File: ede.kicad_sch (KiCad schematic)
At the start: 111 parts, among them J1 Conn_01x01, J10 Conn_01x01, J11 Conn_01x01, J12 Conn_01x01, J2 Conn_01x01, J3 Conn_01x01, J4 Conn_01x01, J5 Conn_01x06, J6 Conn_01x01, J7 Conn_01x04, J8 Conn_01x04, J9 Conn_01x01, Q1 MDP10N027, Q2 MDP10N027, Q3 MDP10N027, Q4 MDP10N027, Q5 MDP10N027, Q6 MDP10N027, U1 Blackpill, U2 NCS20034DR2G, U3 STH0548S12, U4 MP1584EN_4pin, U5 U3216, U6 U3216, U7 U3216

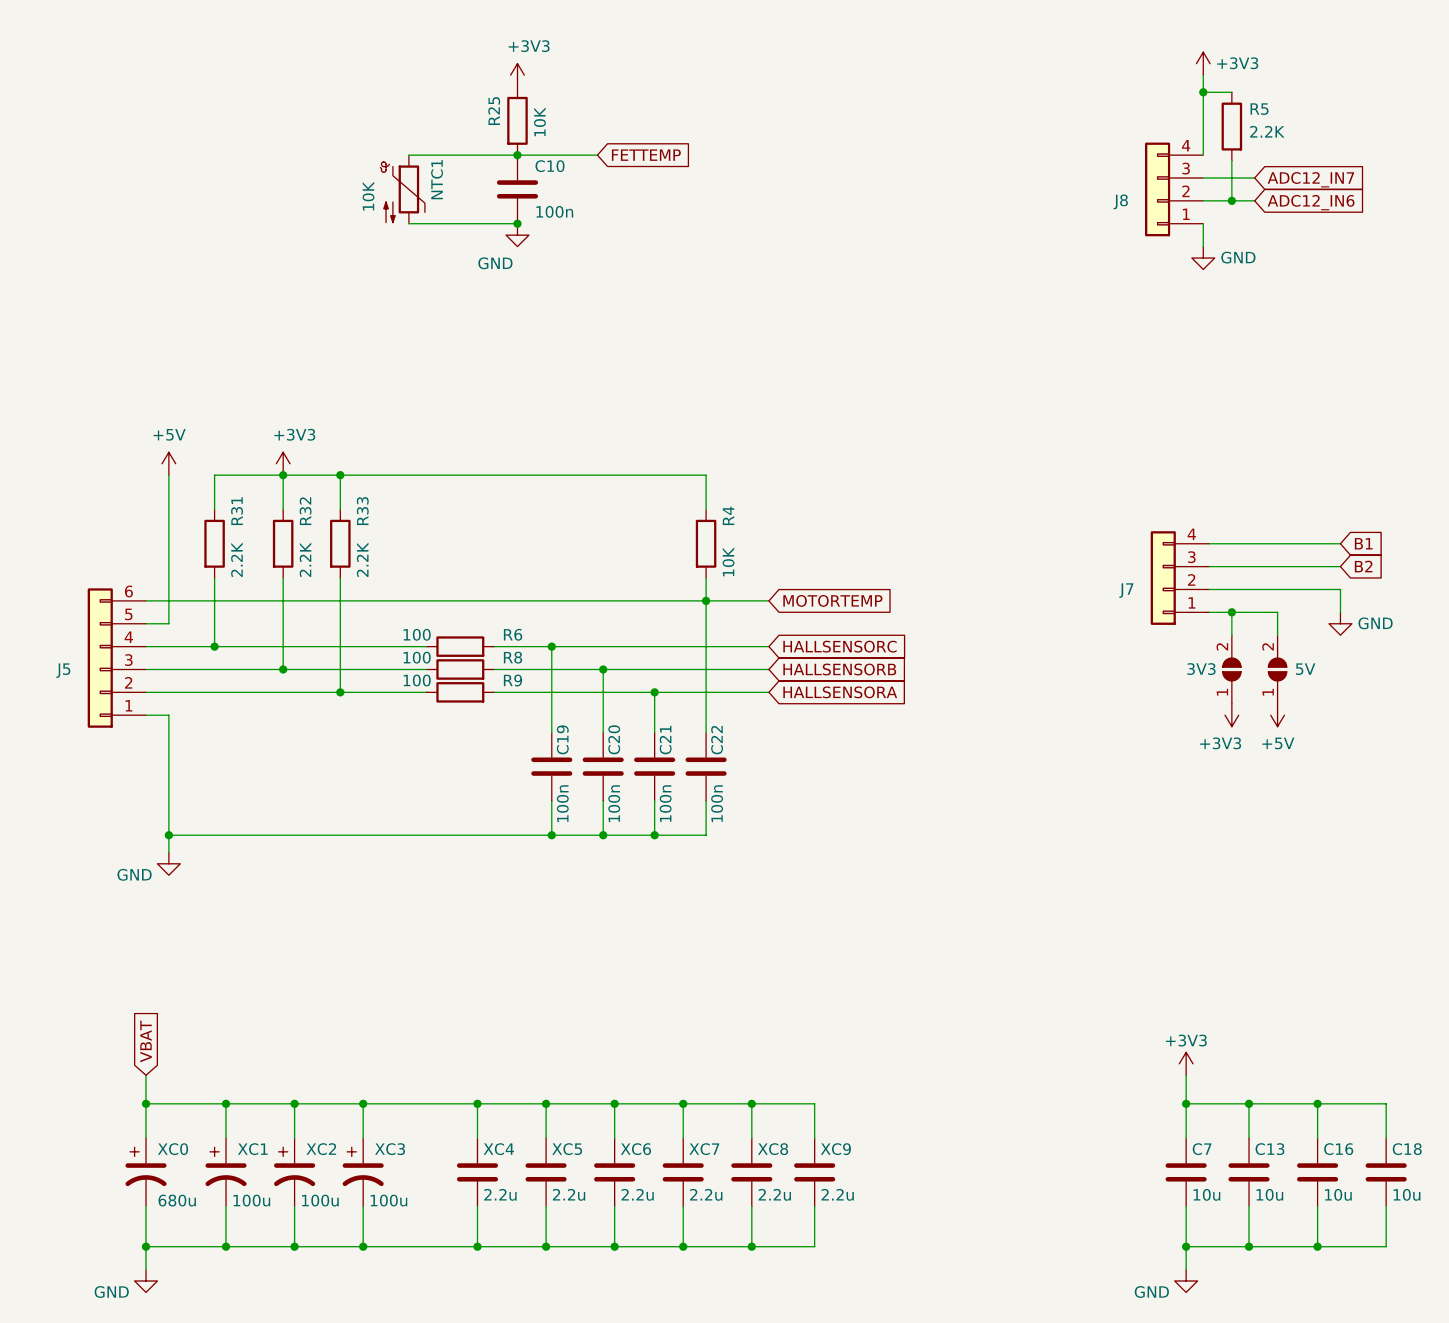
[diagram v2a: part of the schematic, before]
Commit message: KiCad 10 migration
Note: sch & pcb are not in sync, since sch has been changed to represent
blackpill. Though with the existing pcb layout, schematic can be referred,
provided notes mentioned in the schematic are taken into account.

Signed-off-by: Afzal <afzal@intible.in>
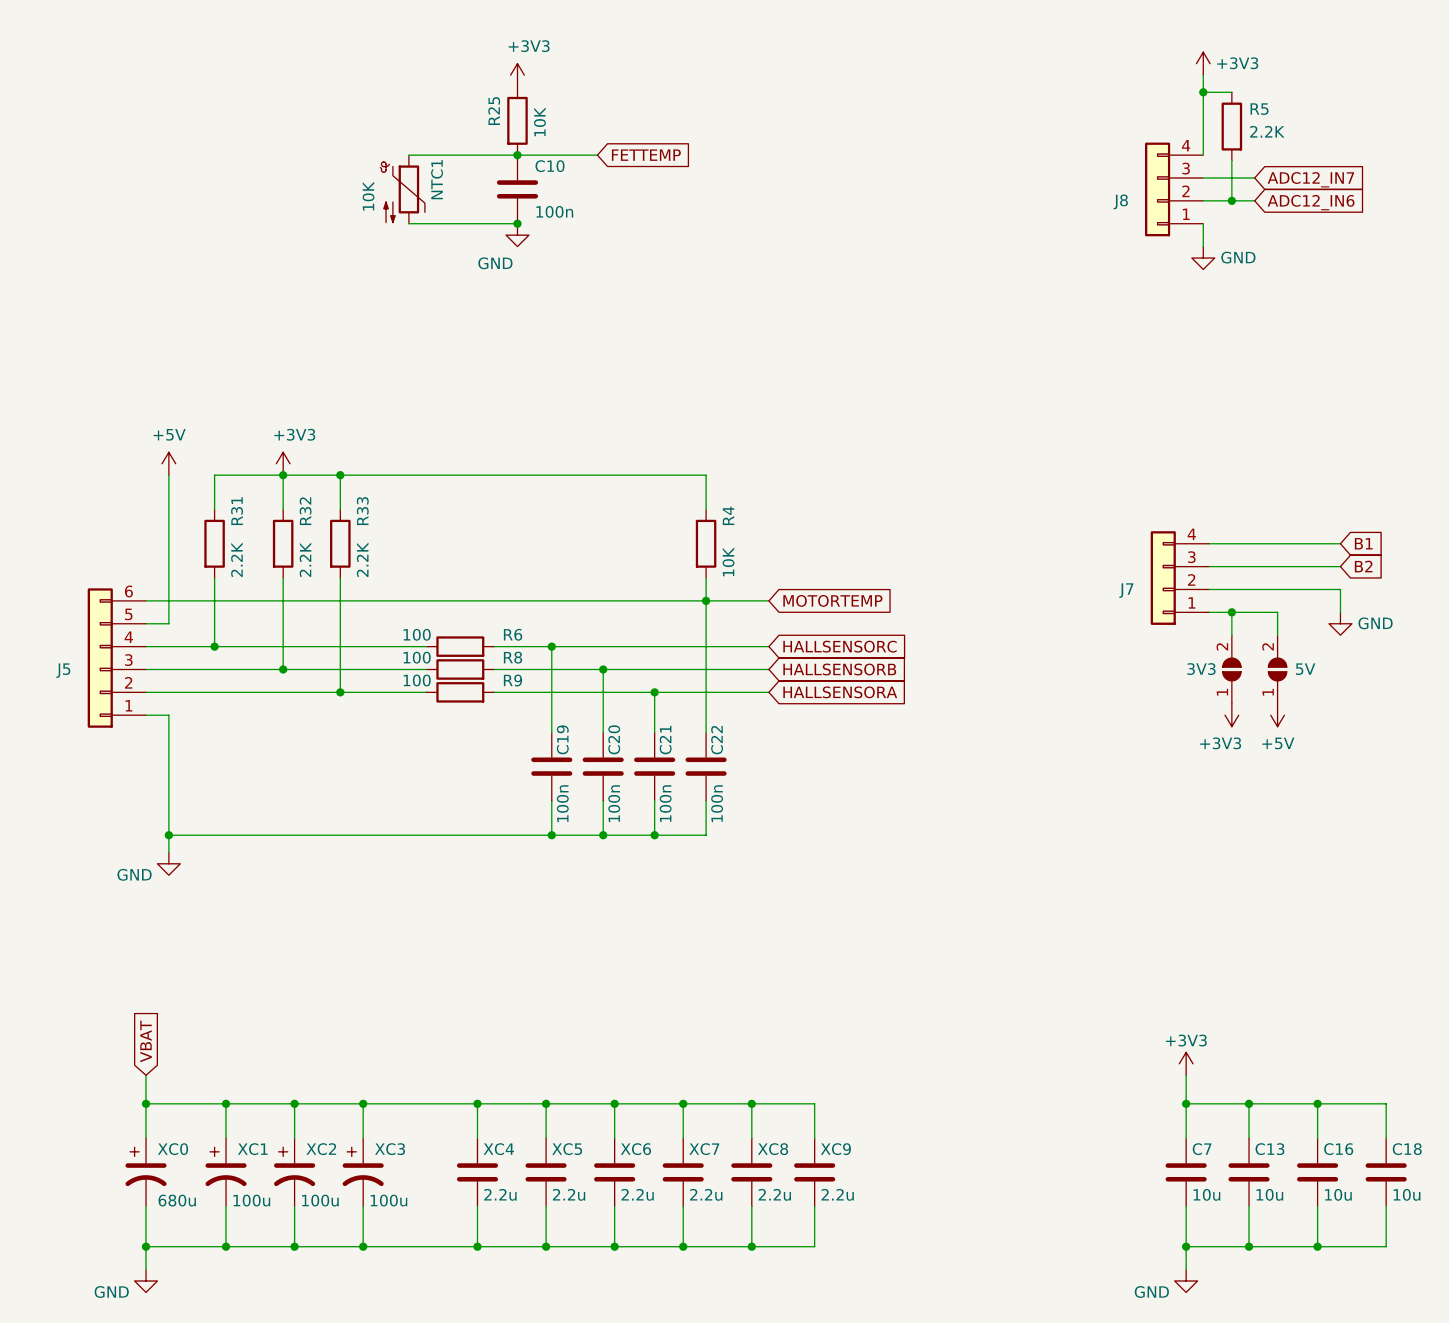
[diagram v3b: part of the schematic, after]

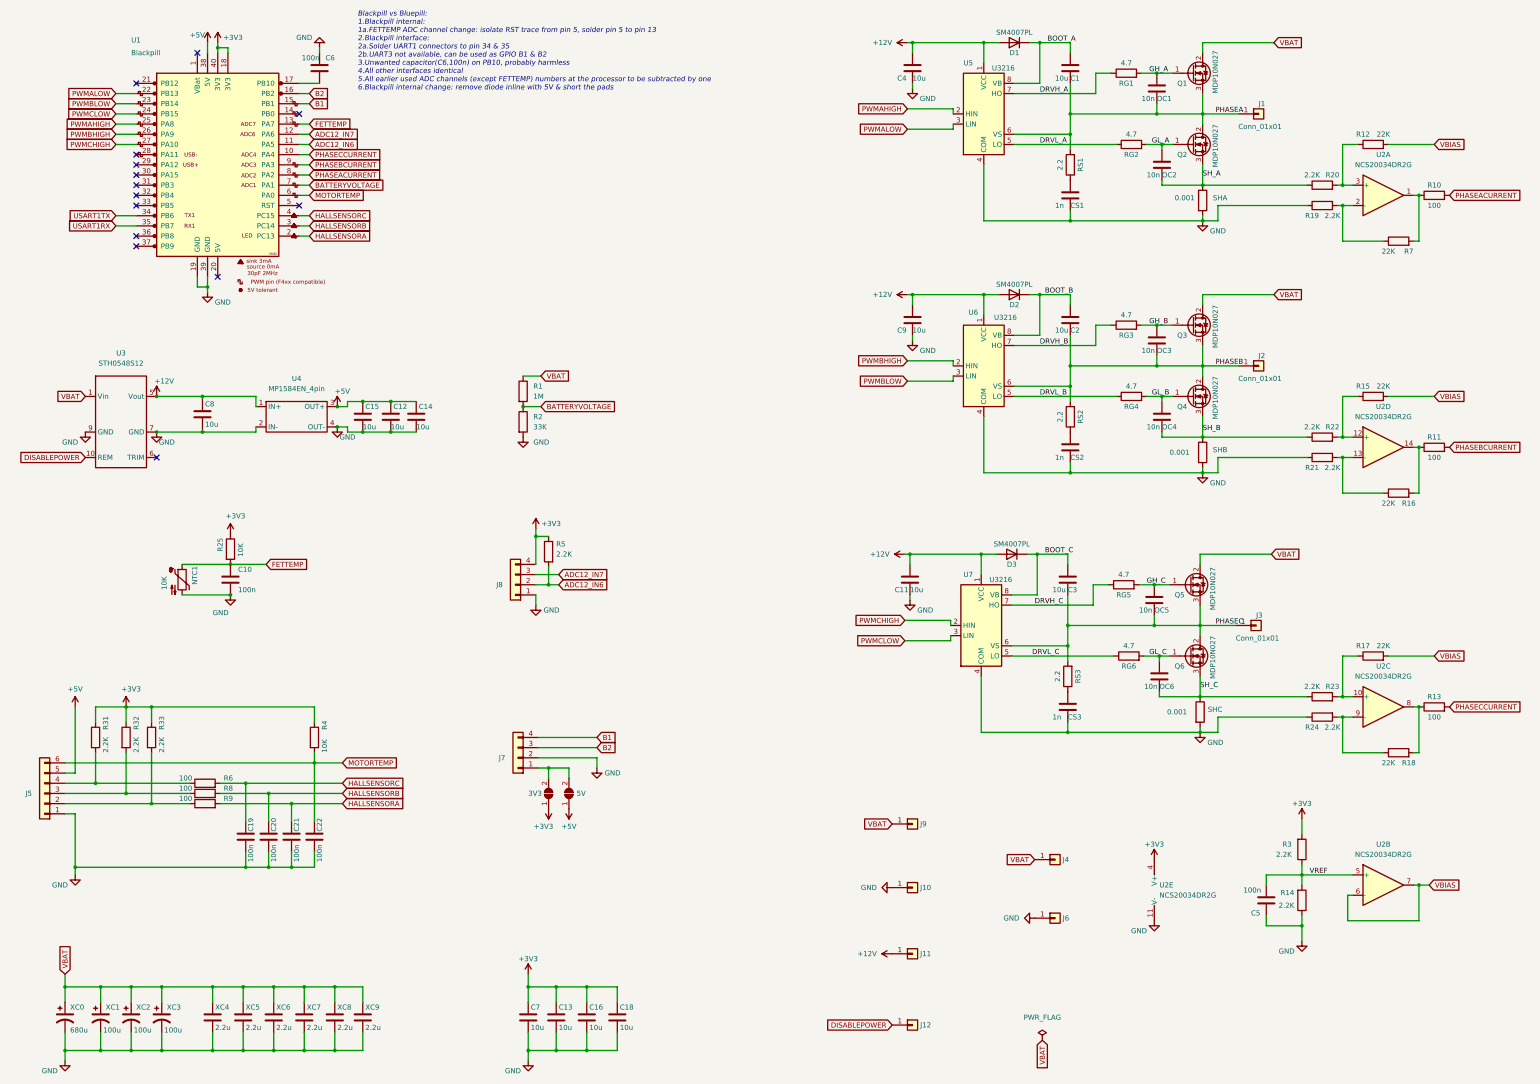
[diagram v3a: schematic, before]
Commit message: sch: align items to grid
Signed-off-by: Afzal <afzal@intible.in>
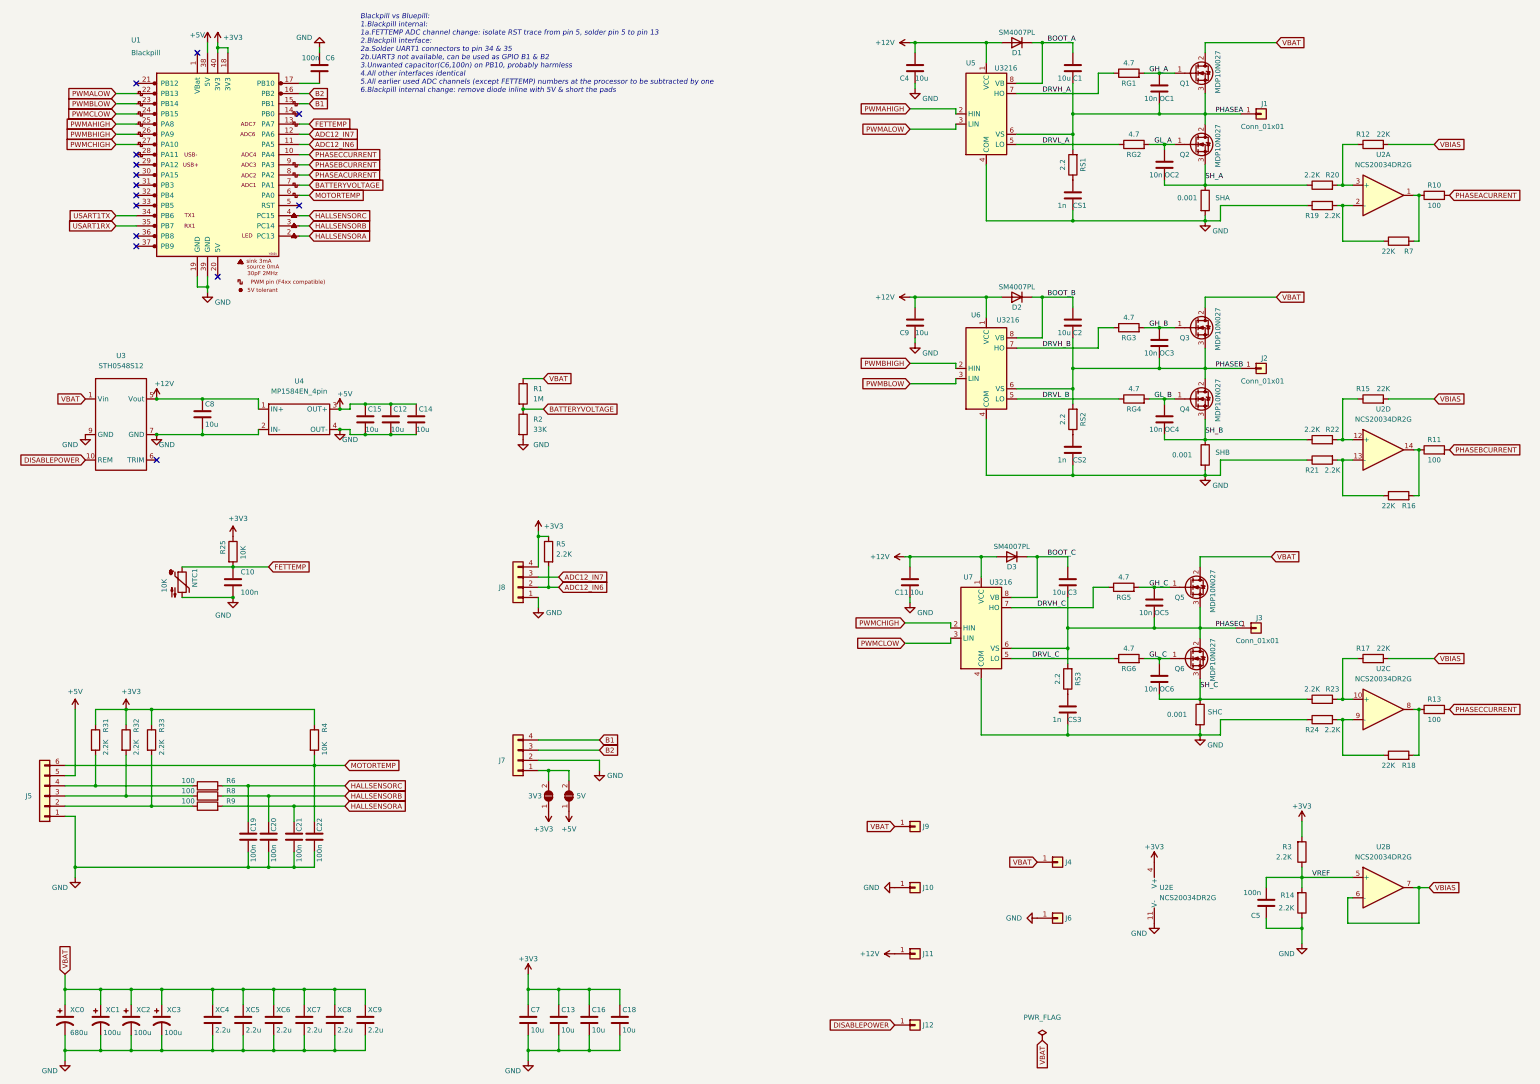
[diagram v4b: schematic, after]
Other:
- moved on the sheet: C1, C10, C11, C12, C13, C14, C15, C16, C18, C19, C2, C21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
